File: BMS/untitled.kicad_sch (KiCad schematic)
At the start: 10 parts, among them Q3 DMT6018LDR-7, Q6 DMT6018LDR-7

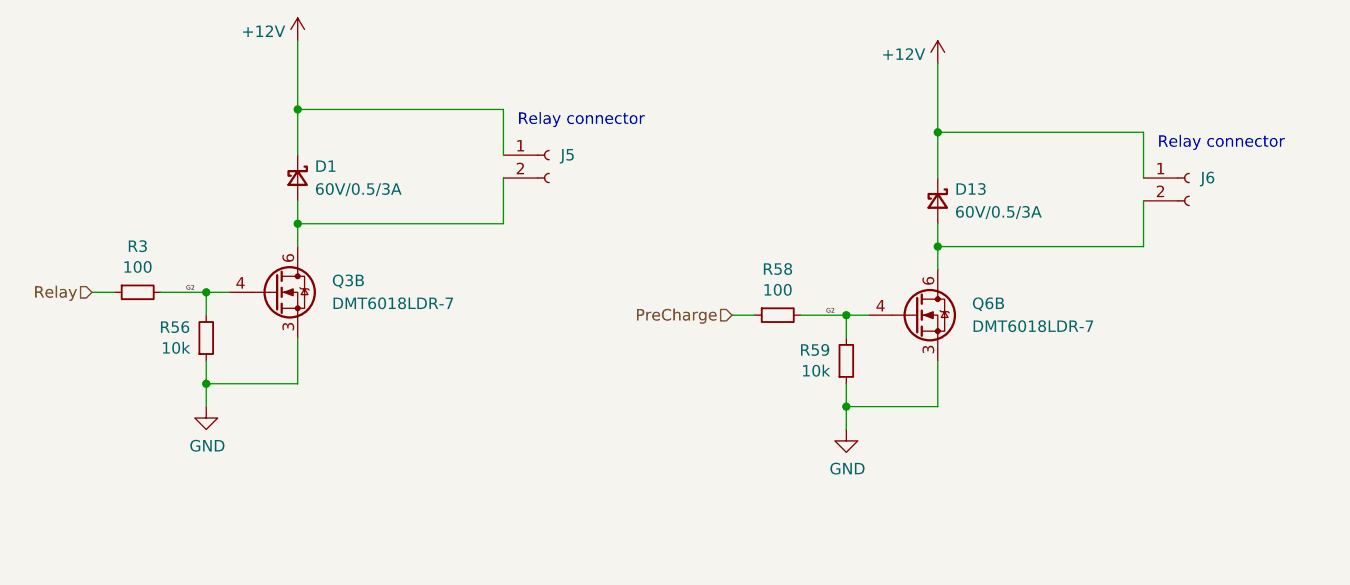
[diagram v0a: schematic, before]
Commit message: Dodano layout drugiego bq79614, ukladu tlumaczącego z protokułu TI na UART oraz wstępnie poprowadzono pary różnicowe
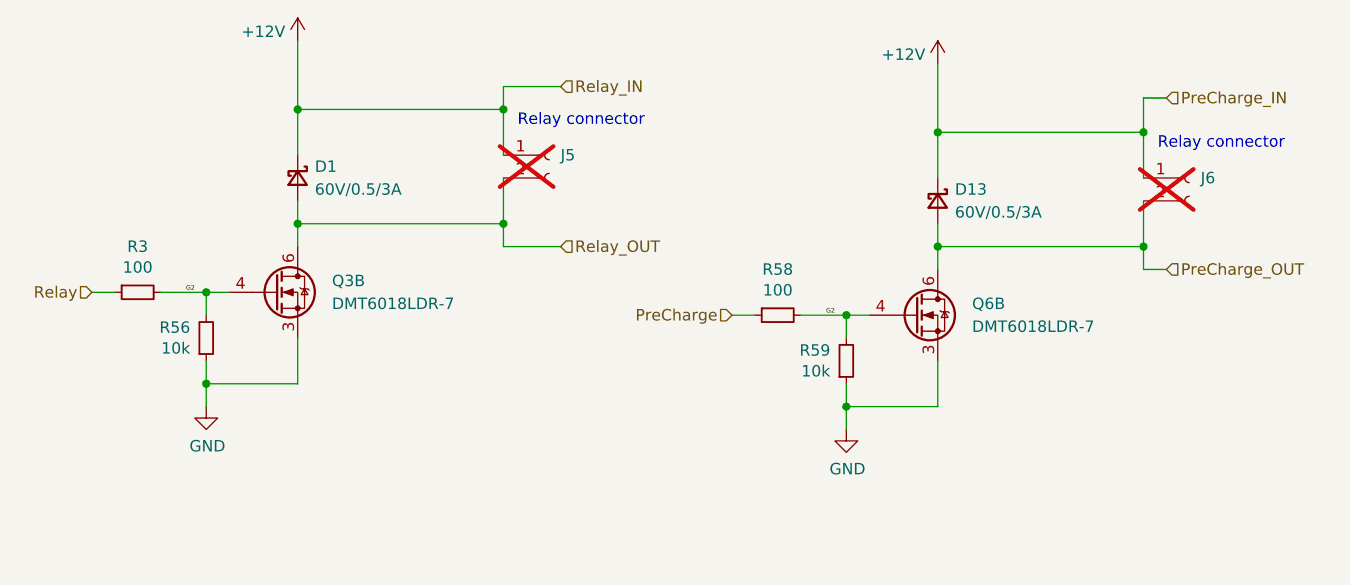
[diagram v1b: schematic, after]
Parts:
- J5, J6: now not fitted; now left out of the parts list
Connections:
- net PreCharge_OUT: now reaches D13.2 (A), J6.2 (Pin_2), Q6.6 (D2)
- net Relay_OUT: now reaches D1.2 (A), J5.2 (Pin_2), Q3.6 (D2)
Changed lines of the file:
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@@
 	(paper "A4")
+	(junction
+		(at 91.44 60.96)
+		(diameter 0)
+		(color 0 0 0 0)
+	)
 	(junction
 		(at 68.58 73.66)
@@
 	)
 	(junction
+		(at 162.56 63.5)
+		(diameter 0)
+		(color 0 0 0 0)
+	)
+	(junction
 		(at 58.42 91.44)
+		(diameter 0)
+		(color 0 0 0 0)
+	)
+	(junction
+		(at 91.44 73.66)
 		(diameter 0)
 		(color 0 0 0 0)
@@
 	)
 	(junction
+		(at 162.56 76.2)
+		(diameter 0)
+		(color 0 0 0 0)
+	)
+	(junction
 		(at 139.7 76.2)
 		(diameter 0)
@@
 	(wire
 		(pts
+			(xy 162.56 78.74) (xy 162.56 76.2)
+		)
+		(stroke
+			(width 0)
+			(type default)
+		)
+	)
+	(wire
+		(pts
 			(xy 91.44 66.04) (xy 91.44 60.96)
 		)
@@
 	(wire
 		(pts
+			(xy 97.79 76.2) (xy 91.44 76.2)
+		)
+		(stroke
+			(width 0)
+			(type default)
+		)
+	)
+	(wire
+		(pts
 			(xy 68.58 60.96) (xy 68.58 66.04)
 		)
@@
 	(wire
 		(pts
+			(xy 165.1 59.69) (xy 162.56 59.69)
+		)
+		(stroke
+			(width 0)
+			(type default)
+		)
+	)
+	(wire
+		(pts
 			(xy 129.54 83.82) (xy 132.08 83.82)
 		)
@@
 	(wire
 		(pts
+			(xy 91.44 58.42) (xy 91.44 60.96)
+		)
+		(stroke
+			(width 0)
+			(type default)
+		)
+	)
+	(wire
+		(pts
+			(xy 165.1 78.74) (xy 162.56 78.74)
+		)
+		(stroke
+			(width 0)
+			(type default)
+		)
+	)
+	(wire
+		(pts
 			(xy 139.7 73.66) (xy 139.7 76.2)
 		)
@@
 	(wire
 		(pts
+			(xy 97.79 58.42) (xy 91.44 58.42)
+		)
+		(stroke
+			(width 0)
+			(type default)
+		)
+	)
+	(wire
+		(pts
 			(xy 129.54 91.44) (xy 129.54 93.98)
 		)
@@
 		(pts
 			(xy 139.7 63.5) (xy 162.56 63.5)
+		)
+		(stroke
+			(width 0)
+			(type default)
+		)
+	)
+	(wire
+		(pts
+			(xy 162.56 59.69) (xy 162.56 63.5)
+		)
+		(stroke
+			(width 0)
+			(type default)
+		)
+	)
+	(wire
+		(pts
+			(xy 91.44 76.2) (xy 91.44 73.66)
 		)
 		(stroke
@@
 		)
 	)
+	(hierarchical_label "Relay_IN"
+		(shape input)
+		(at 97.79 58.42 0)
+		(fields_autoplaced yes)
+		(effects
+			(font
+				(size 1.27 1.27)
+			)
+			(justify left)
+		)
+	)
+	(hierarchical_label "PreCharge_OUT"
+		(shape input)
+		(at 165.1 78.74 0)
+		(fields_autoplaced yes)
+		(effects
+			(font
+				(size 1.27 1.27)
+			)
+			(justify left)
+		)
+	)
+	(hierarchical_label "PreCharge_IN"
+		(shape input)
+		(at 165.1 59.69 0)
+		(fields_autoplaced yes)
+		(effects
+			(font
+				(size 1.27 1.27)
+			)
+			(justify left)
+		)
+	)
 	(hierarchical_label "Relay"
 		(shape input)
@@
 			)
 			(justify right)
+		)
+	)
+	(hierarchical_label "Relay_OUT"
+		(shape input)
+		(at 97.79 76.2 0)
+		(fields_autoplaced yes)
+		(effects
+			(font
+				(size 1.27 1.27)
+			)
+			(justify left)
 		)
 	)
@@
 		(at 167.64 68.58 0)
 		(unit 1)
-		(exclude_from_sim no)
-		(in_bom yes)
-		(on_board yes)
-		(dnp no)
+		(exclude_from_sim yes)
+		(in_bom no)
+		(on_board no)
+		(dnp yes)
 		(fields_autoplaced yes)
 		(property "Reference" "J6"
@@
 		(at 96.52 66.04 0)
 		(unit 1)
-		(exclude_from_sim no)
-		(in_bom yes)
-		(on_board yes)
-		(dnp no)
+		(exclude_from_sim yes)
+		(in_bom no)
+		(on_board no)
+		(dnp yes)
 		(fields_autoplaced yes)
 		(property "Reference" "J5"

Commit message: Iteracja 1.0 gotowa, teraz sprawdzenie i zmiany kosmetyczne
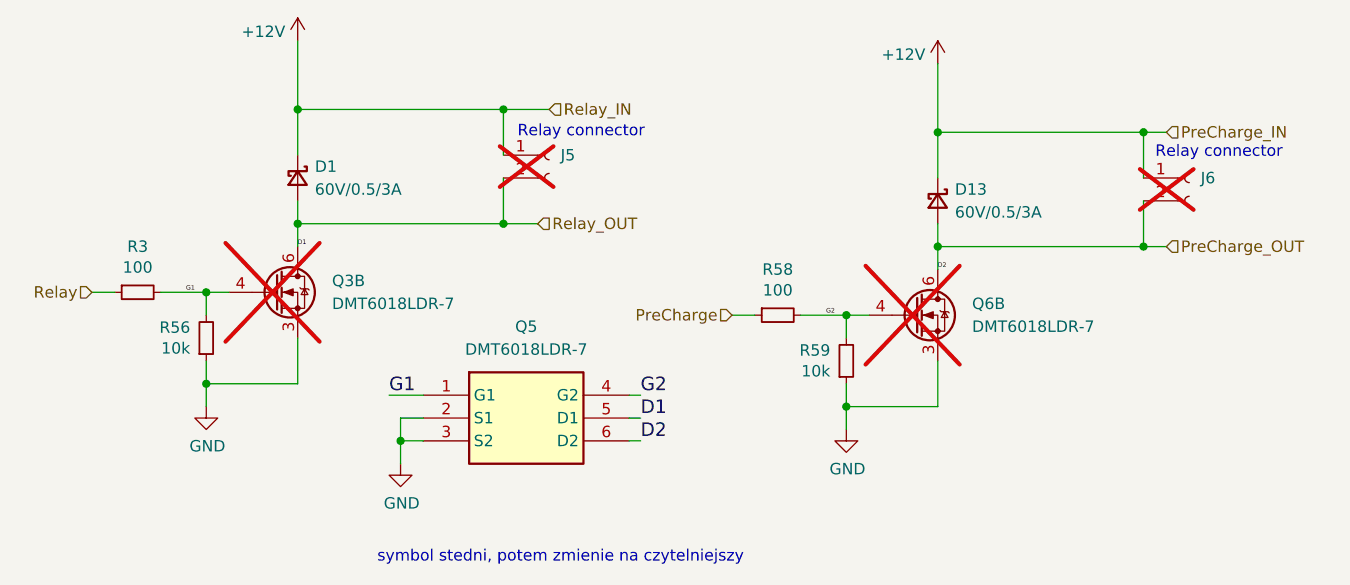
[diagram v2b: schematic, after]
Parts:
- added Q5: DMT6018LDR-7, DMT6018LDR7, symbol DMT6018LDR-7:DMT6018LDR-7
- Q3, Q6: now not fitted; now left out of the parts list
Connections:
- net G2: now also Q5.4 (G2); no longer Q3.4 (G2), R3.2, R56.2
- net GND: now also Q5.2 (S1), Q5.3 (S2)
- net PreCharge_OUT: now also Q5.6 (D2)
- net Relay_OUT: now also Q5.5 (D1)
- new net G1: Q3.4 (G2), Q5.1 (G1), R3.2, R56.2
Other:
- note added: "symbol stedni, potem zmienie na czytelniejszy"
